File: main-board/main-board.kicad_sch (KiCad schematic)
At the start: 41 parts, among them J1 Conn_02x08_Odd_Even, J2 Bat, Q1 AO3400A, Q2 AO3400A, Q3 AO3400A, Q4 AO3400A, Q5 AO3400A, Q6 AO3400A, Q7 AO3400A, Q8 AO3400A, U1 40106, U2 4024, U3 4040, U4 27C256, U5 LM78L05, U6 ULN2803A, U7 4028

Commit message: Finalized Rev-1.0
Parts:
- added D2: LED, LED_THT:LED_D3.0mm, symbol Device:LED
- added R12: 360, Resistor_THT:R_Axial_DIN0207_L6.3mm_D2.5mm_P10.16mm_Horizontal, symbol Device:R
- added TP1, TP2, TP3, TP4: TestPoint, ezee-footprints:TestPoint_Pad_D1.0mm, symbol Connector:TestPoint
- added TPH1, TPH2: TestPoint_Hook, ezee-footprints:TestPoint_Hook, symbol ezee-symbols:TestPoint_Hook
- added U9: L7805, Package_TO_SOT_THT:TO-220-3_Vertical, symbol Regulator_Linear:L7805
- FID1, FID2, FID3, MH1, MH2, MH3, MH4: now not fitted
- J1: now not fitted; now left out of the parts list
- J2: value Bat -> 7-12V; now not fitted; now left out of the parts list
- Q1: Attrition Qty 4 -> (none); Category Transistors,MOSFETs -> (none); Class Basic Component -> (none); Continuous Drain Current (Id) 5.7A -> (none); Drain Source On Resistance (RDS(on)@Vgs,Id) 26.5mΩ@10V,5.7A -> (none); Drain Source Voltage (Vdss) 30V -> (none); Gate Threshold Voltage (Vgs(th)@Id) 1.5V@250uA -> (none); Input Capacitance (Ciss@Vds) 630pF@15V -> (none); LCSC C20917 -> (none); Manufacturer Alpha & Omega Semicon -> (none); Minimum Qty 5 -> (none); Operating Temperature -55°C~+150°C@(Tj) -> (none); Part AO3400A -> (none); Power Dissipation (Pd) 1.4W -> (none); Price 0.074USD -> (none); Process SMT -> (none); Stock 463122 -> (none); Total Gate Charge (Qg@Vgs) 7nC@4.5V -> (none); Type 1 N-channel -> (none)
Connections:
- net +5V: now also D2.2 (A), U9.3 (OUT)
- net GND: now also R12.1, TPH2.1, U9.2 (GND)
- net at U1.4, U2.1 (~{CLK}): now also TP1.1
- net at U1.8, U3.10 (CLK): now also TP2.1
- net at D1.1 (K), U5.3 (VI): now also U9.1 (IN)
- net at D1.2 (A), J2.1 (Pin_1): now also TPH1.1
- net at J1.1 (Pin_1), Q1.2 (S): now also TP3.1
- net at J1.2 (Pin_2), R11.2: now also TP4.1
- new net: D2.1 (K), R12.2
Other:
- note added: "TO-220"
- note added: "TO-92"
- note removed: "3 Fiducials/component-layer"

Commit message: fixed 2n7000 footprint and added testpoints
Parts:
- removed Q1, Q2, Q3, Q4, Q5, Q6, Q7, Q8: AO3400A, Package_TO_SOT_THT:TO-92, symbol PCM_JLCPCB-Transistors:NMOS,AO3400A
- added Q1, Q2, Q3, Q4, Q5, Q6, Q7, Q8: 2N7000, Package_TO_SOT_THT:TO-92_Inline, symbol Transistor_FET:2N7000
- added TP3, TP4, TP5, TP6, TP7, TP8, TP9: TestPoint, ezee-footprints:TestPoint_Pad_D1.0mm, symbol Connector:TestPoint
- C1, C5: value 0.1u -> 0.22u
- R1: value 8.2k -> 12k
- R10, R11, R4, R5, R6, R7, R8, R9: value 330 -> 360
- renumbered TP3 to TP1, TP1 to TP10, TP2 to TP11, TP4 to TP2
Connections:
- net +5V: now also Q1.3 (D), Q2.3 (D), Q3.3 (D), Q4.3 (D), Q5.3 (D), Q6.3 (D), Q7.3 (D), Q8.3 (D)
- net at U4.18 (D6): now also Q7.2 (G)
- net at J1.13 (Pin_13): now also Q7.1 (S), TP7.1
- net at J1.2 (Pin_2), R11.2: now also TP9.1; no longer TP2.1
- net at U4.11 (D0): now also Q1.2 (G)
- net at U4.12 (D1): now also Q2.2 (G)
- net at U4.13 (D2): now also Q3.2 (G)
- net at U4.15 (D3): now also Q4.2 (G)
- net at U4.16 (D4): now also Q5.2 (G)
- net at U4.17 (D5): now also Q6.2 (G)
- net at U4.19 (D7): now also Q8.2 (G)
- net at J1.15 (Pin_15): now also Q8.1 (S), TP8.1
- net at J1.7 (Pin_7): now also Q4.1 (S), TP4.1
- net at J1.3 (Pin_3): now also TP2.1, Q2.1 (S)
- net at J1.9 (Pin_9): now also Q5.1 (S), TP5.1
- net at J1.1 (Pin_1), TP1.1: now also Q1.1 (S)
- net at J1.11 (Pin_11): now also Q6.1 (S), TP6.1
- net at J1.5 (Pin_5): now also Q3.1 (S), TP3.1
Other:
- note added: "I(led) = 5V-1.7V/360 = 12.6mA"
- note added: "f = 1/(12000*0.2E-6) = 378Hz"
- note removed: "I(led) = 5V-2V/330 = 10mA"
- note removed: "f = 1/(8200*0.1E-6) = 554Hz"
- moved on the sheet: TP2

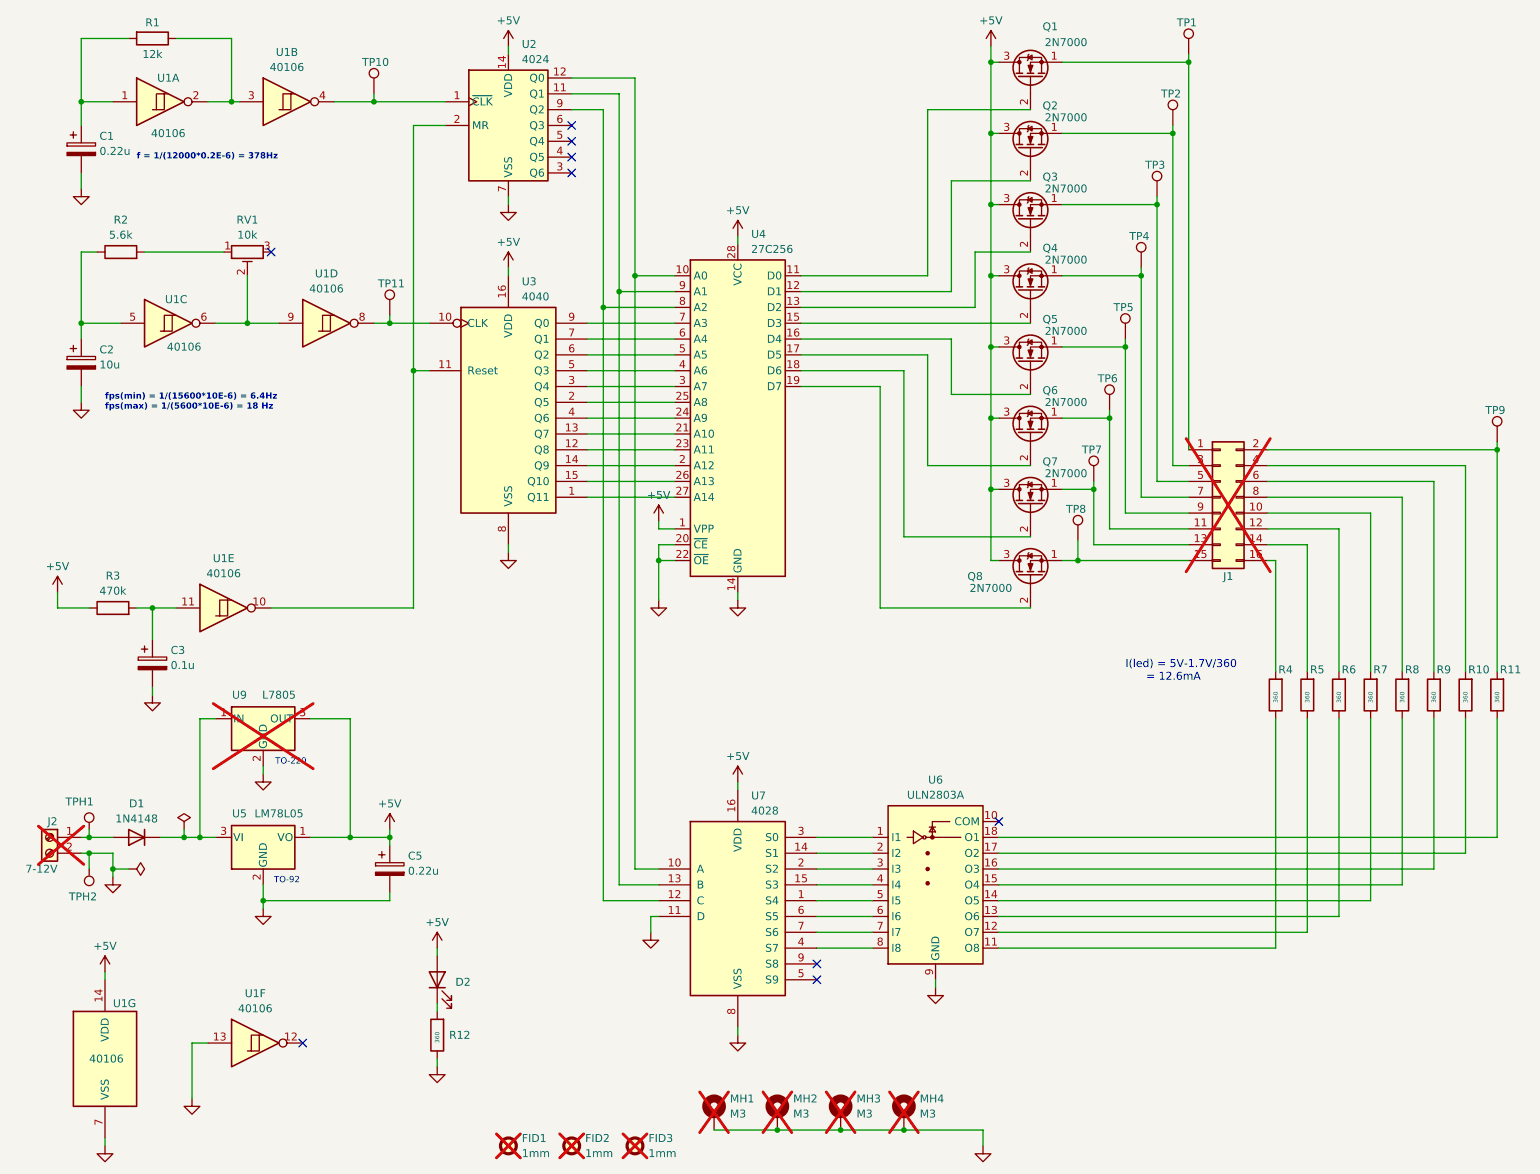
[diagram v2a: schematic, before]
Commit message: started smd conversion
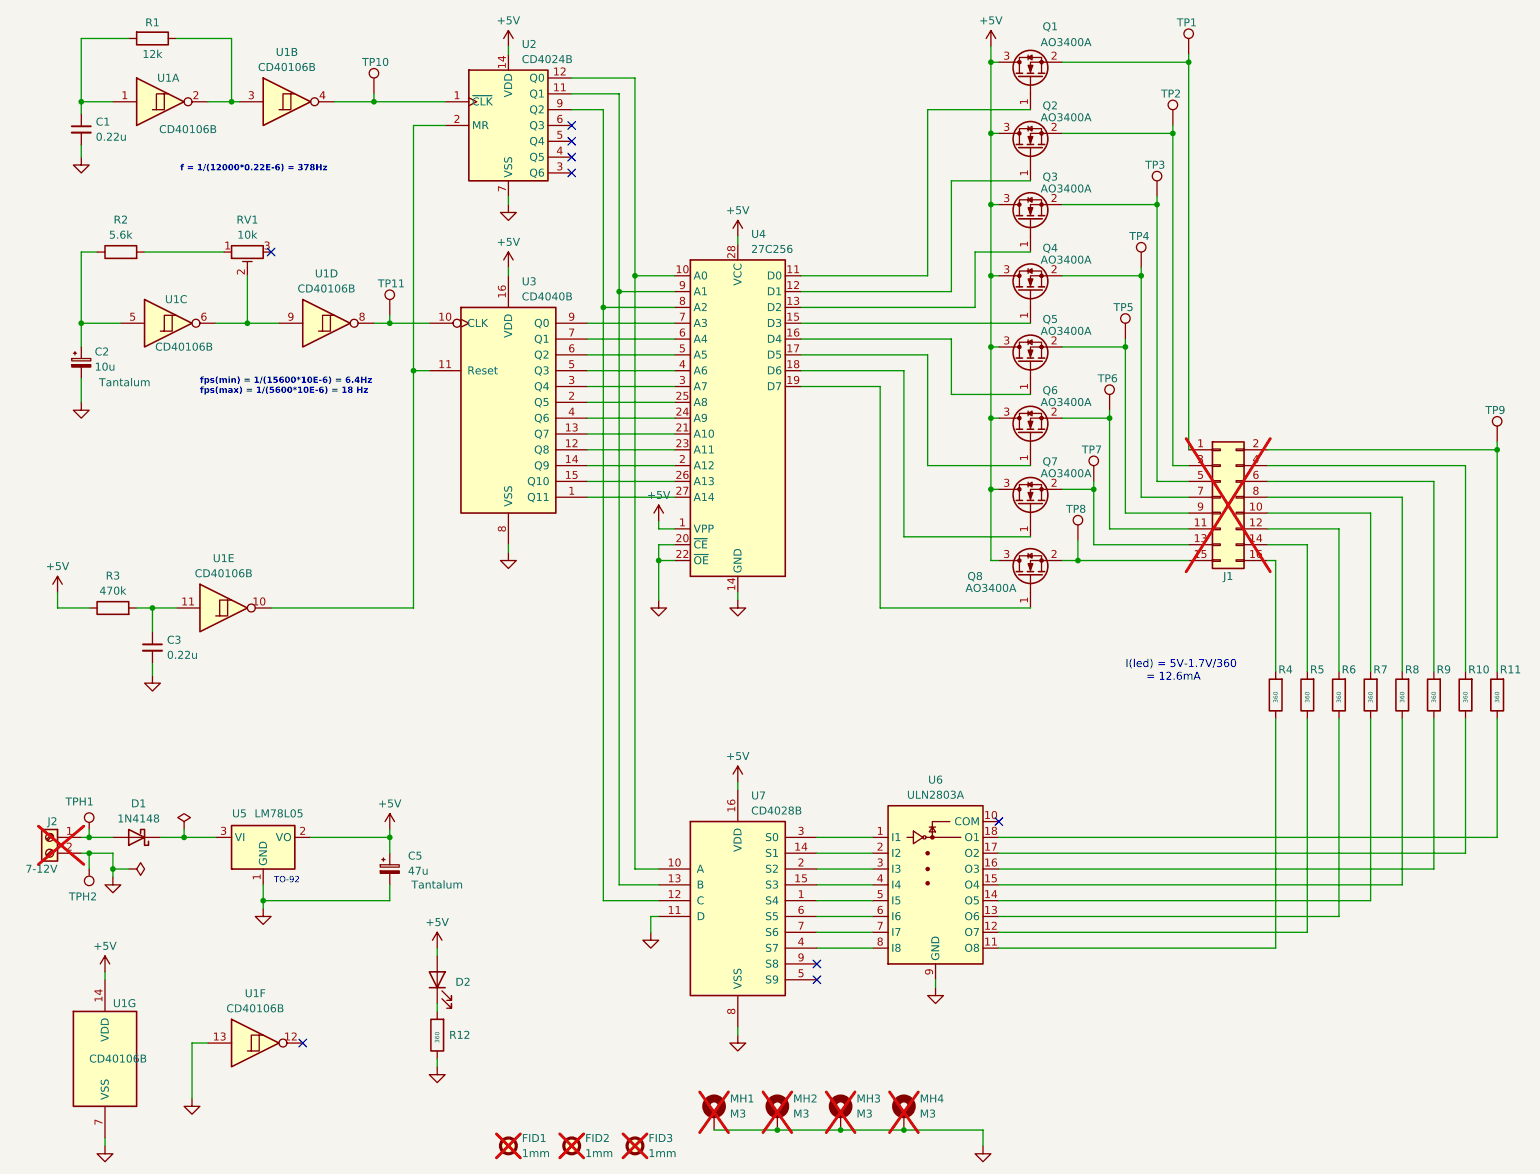
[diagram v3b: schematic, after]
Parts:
- removed U9: L7805, Package_TO_SOT_THT:TO-220-3_Vertical, symbol Regulator_Linear:L7805
- C1: footprint Capacitor_THT:CP_Radial_D4.0mm_P1.50mm -> Capacitor_SMD:C_0603_1608Metric_Pad1.08x0.95mm_HandSolder; symbol Device:C_Polarized -> Device:C_Small
- C2: footprint Capacitor_THT:CP_Radial_D4.0mm_P1.50mm -> Capacitor_Tantalum_SMD:CP_EIA-7343-20_Kemet-V; symbol Device:C_Polarized -> Device:C_Polarized_Small
- C3: value 0.1u -> 0.22u; footprint Capacitor_THT:CP_Radial_D4.0mm_P1.50mm -> Capacitor_SMD:C_0603_1608Metric_Pad1.08x0.95mm_HandSolder; symbol Device:C_Polarized -> Device:C_Small
- C5: value 0.22u -> 47u; footprint Capacitor_THT:CP_Radial_D4.0mm_P1.50mm -> Capacitor_Tantalum_SMD:CP_EIA-7343-20_Kemet-V; symbol Device:C_Polarized -> Device:C_Polarized_Small
- D1: footprint Diode_THT:D_DO-35_SOD27_P7.62mm_Horizontal -> Diode_SMD:D_SMA; symbol Diode:1N4148 -> Diode:SS12
- D2: footprint LED_THT:LED_D3.0mm -> LED_SMD:LED_0805_2012Metric_Pad1.15x1.40mm_HandSolder
- Q1, Q2, Q3, Q4, Q5, Q6, Q7, Q8: value 2N7000 -> AO3400A; footprint Package_TO_SOT_THT:TO-92_Inline -> Package_TO_SOT_SMD:SOT-23; symbol Transistor_FET:2N7000 -> Transistor_FET:AO3400A
- R1: footprint Resistor_THT:R_Axial_DIN0207_L6.3mm_D2.5mm_P10.16mm_Horizontal -> Resistor_SMD:R_0603_1608Metric_Pad0.98x0.95mm_HandSolder
- R10, R11, R12, R2, R3, R4, R5, R6, R7, R8, R9: footprint Resistor_THT:R_Axial_DIN0207_L6.3mm_D2.5mm_P10.16mm_Horizontal -> Capacitor_SMD:C_0603_1608Metric_Pad1.08x0.95mm_HandSolder
- U1: value 40106 -> CD40106B; footprint Package_DIP:DIP-14_W7.62mm -> Package_SO:SOIC-14_3.9x8.7mm_P1.27mm
- U2: value 4024 -> CD4024B; footprint Package_DIP:DIP-14_W7.62mm -> Package_SO:SOIC-14_3.9x8.7mm_P1.27mm
- U3: value 4040 -> CD4040B; footprint Package_DIP:DIP-16_W7.62mm -> Package_SO:SOIC-16_3.9x9.9mm_P1.27mm
- U5: footprint Package_TO_SOT_THT:TO-92_Inline -> Package_TO_SOT_SMD:SOT-223-3_TabPin2; symbol Regulator_Linear:LM78L05_TO92 -> Regulator_Linear:AMS1117-5.0
- U6: footprint Package_DIP:DIP-18_W7.62mm -> Package_SO:SSOP-18_4.4x6.5mm_P0.65mm
- U7: value 4028 -> CD4028B; footprint Package_DIP:DIP-16_W7.62mm -> Package_SO:SOIC-16_3.9x9.9mm_P1.27mm
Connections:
- net +5V: now also U5.2 (VO); no longer U5.1 (VO)
- net GND: now also U5.1 (GND); no longer U5.2 (GND)
- net at J1.13 (Pin_13), TP7.1: now also Q7.2 (S); no longer Q7.1 (S)
- net at J1.5 (Pin_5), TP3.1: now also Q3.2 (S); no longer Q3.1 (S)
- net at U4.13 (D2): now also Q3.1 (G); no longer Q3.2 (G)
- net at J1.3 (Pin_3), TP2.1: now also Q2.2 (S); no longer Q2.1 (S)
- net at U4.11 (D0): now also Q1.1 (G); no longer Q1.2 (G)
- net at U4.12 (D1): now also Q2.1 (G); no longer Q2.2 (G)
- net at U4.15 (D3): now also Q4.1 (G); no longer Q4.2 (G)
- net at U4.16 (D4): now also Q5.1 (G); no longer Q5.2 (G)
- net at U4.17 (D5): now also Q6.1 (G); no longer Q6.2 (G)
- net at U4.18 (D6): now also Q7.1 (G); no longer Q7.2 (G)
- net at U4.19 (D7): now also Q8.1 (G); no longer Q8.2 (G)
- net at J1.11 (Pin_11), TP6.1: now also Q6.2 (S); no longer Q6.1 (S)
- net at J1.15 (Pin_15), TP8.1: now also Q8.2 (S); no longer Q8.1 (S)
- net at J1.7 (Pin_7), TP4.1: now also Q4.2 (S); no longer Q4.1 (S)
- net at J1.1 (Pin_1), TP1.1: now also Q1.2 (S); no longer Q1.1 (S)
- net at J1.9 (Pin_9), TP5.1: now also Q5.2 (S); no longer Q5.1 (S)
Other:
- note added: "f = 1/(12000*0.22E-6) = 378Hz"
- note removed: "TO-220"
- note removed: "f = 1/(12000*0.2E-6) = 378Hz"

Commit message: docs
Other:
- note added: "ALLE FOOTPRINTS ENDRET"
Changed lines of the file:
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@@
+		)
+	)
+	(text "ALLE FOOTPRINTS ENDRET"
+		(exclude_from_sim no)
+		(at 62.23 127.635 0)
+		(effects
+			(font
+				(size 4 4)
+				(thickness 0.8)
+				(bold yes)
+			)
 		)
 	)
